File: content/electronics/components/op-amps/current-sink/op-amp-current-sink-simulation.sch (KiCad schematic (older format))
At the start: 6 parts, among them M1 2N7002, U1 AD8009

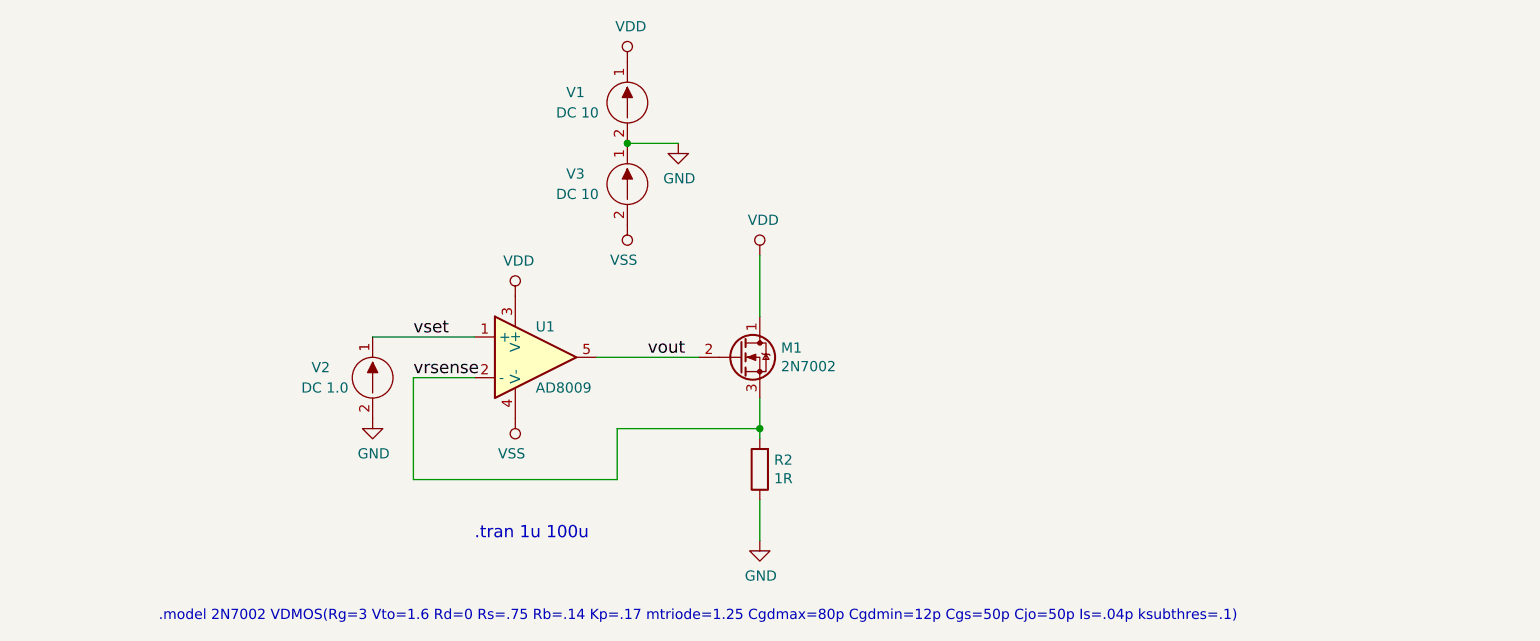
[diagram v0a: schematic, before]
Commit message: Updated the simulation section on the KiCad page.
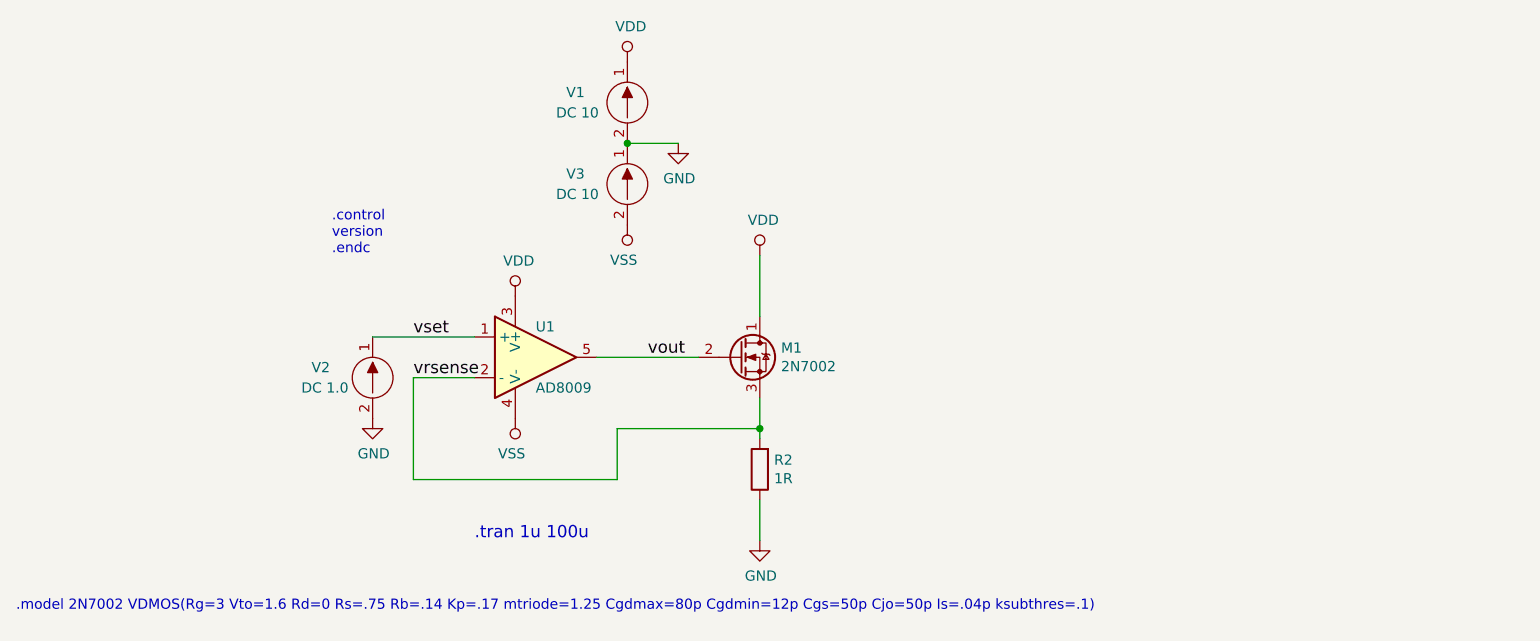
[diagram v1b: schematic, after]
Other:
- note added: ".control\nversion\n.endc"
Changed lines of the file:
@@
 Text Label 4300 3750 0    60   ~ 0
 vrsense
-Text Notes 3050 4950 0    50   ~ 0
+Text Notes 2350 4900 0    50   ~ 0
 .model 2N7002 VDMOS(Rg=3 Vto=1.6 Rd=0 Rs=.75 Rb=.14 Kp=.17 mtriode=1.25 Cgdmax=80p Cgdmin=12p Cgs=50p Cjo=50p Is=.04p ksubthres=.1)
 $Comp
@@
 Wire Wire Line
 	6000 3850 6000 4000
+Text Notes 3900 3150 0    50   ~ 0
+.control\nversion\n.endc
 $EndSCHEMATC
